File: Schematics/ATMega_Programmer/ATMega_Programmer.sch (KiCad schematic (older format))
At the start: 22 parts, among them U1 74HC04, U2 ATmega644PA, U3 74HC04, U4 28C256, U5 74HC595, U6 74HC00, U7 74LVC1G157, U8 74LVC1G157, U9 74LVC1G126, Y1 20MHz

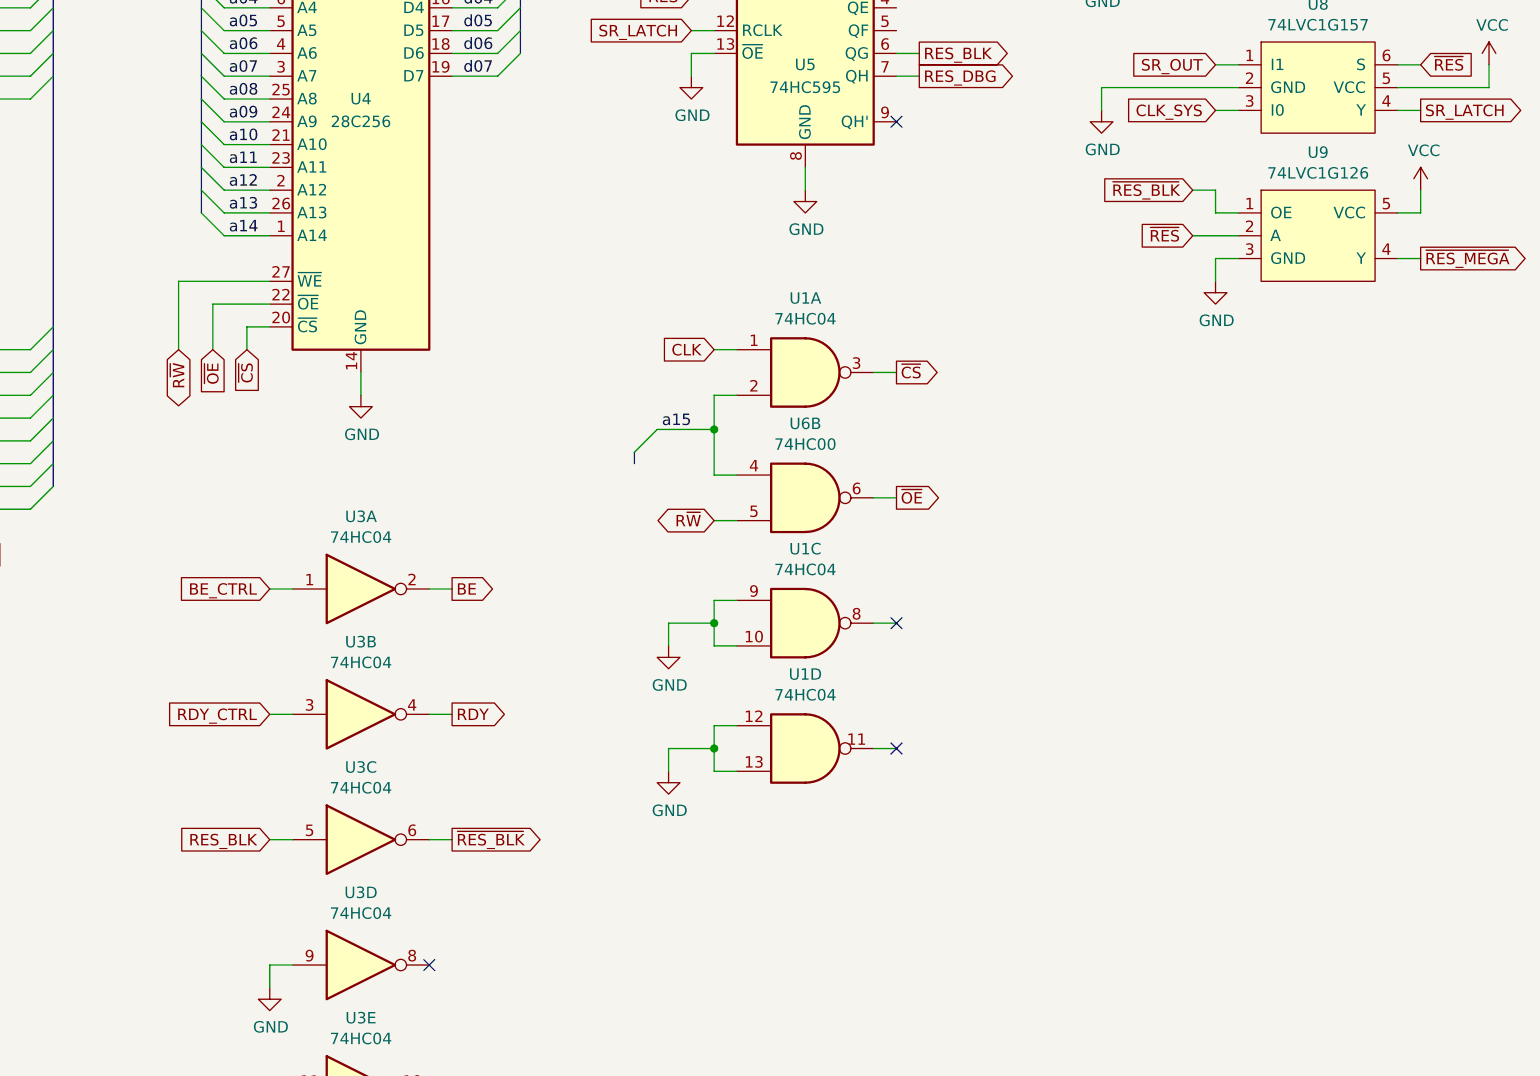
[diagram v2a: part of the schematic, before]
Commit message: Changed 74LVC1G126 to 74LVC1G125 for low-active OE
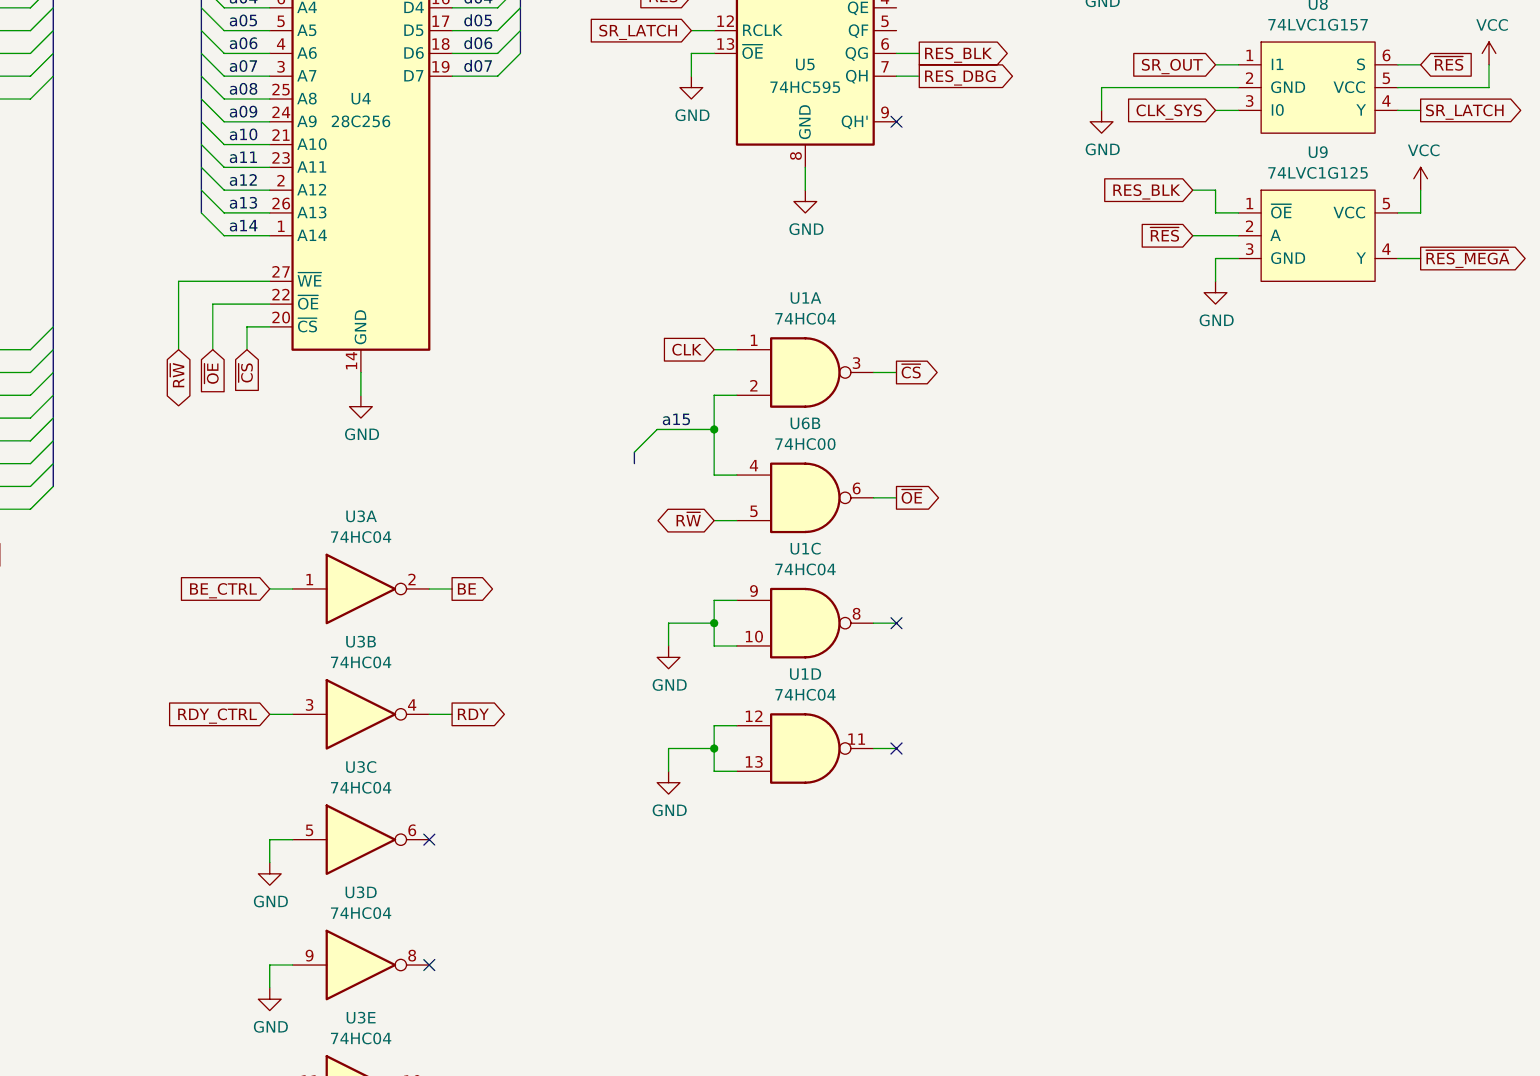
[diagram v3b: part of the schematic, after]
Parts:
- removed U7, U8: 74LVC1G157, Package_SO:SC-74-6_1.5x2.9mm_P0.95mm, symbol 74LVC1G157:74LVC1G157
- removed U9: 74LVC1G126, Package_SO:SC-74-6_1.5x2.9mm_P0.95mm, symbol 74LVC1G126:74LVC1G126
- added U7, U8: 74LVC1G157, Package_SO:SC-74-6_1.5x2.9mm_P0.95mm, symbol 74LVC1G:74LVC1G157
- added U9: 74LVC1G125, Package_SO:SC-74-6_1.5x2.9mm_P0.95mm, symbol 74LVC1G:74LVC1G125
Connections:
- net CLK: now also U7.4 (Y)
- net CLKSEL: now also U7.6 (S)
- net CLK_DBG: now also U7.1 (I1)
- net CLK_SYS: now also U7.3 (I0), U8.3 (I0)
- net GND: now also U3.5, U7.2 (GND), U8.2 (GND), U9.3 (GND)
- net RES_BLK: now also U9.1 (~OE); no longer U3.5
- net SR_LATCH: now also U8.4 (Y)
- net SR_OUT: now also U8.1 (I1)
- net VCC: now also U7.5 (VCC), U8.5 (VCC), U9.5 (VCC)
- net ~RES: now also U8.6 (S), U9.2 (A)
- net ~RES_MEGA: now also U9.4 (Y)
- net ~RES_BLK: no longer names the net of U3.6
- no-connect marks 6 -> 7
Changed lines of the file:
@@
 $EndComp
 $Comp
-L power:GND #PWR015
+L power:GND #PWR016
 U 1 1 5F38A5CE
 P 5550 3350
-F 0 "#PWR015" H 5550 3100 50  0001 C CNN
+F 0 "#PWR016" H 5550 3100 50  0001 C CNN
 F 1 "GND" H 5555 3177 50  0000 C CNN
 F 2 "" H 5550 3350 50  0001 C CNN
@@
 	2850 950  2850 850
 $Comp
-L power:VCC #PWR014
+L power:VCC #PWR015
 U 1 1 5F39AD33
 P 5550 950
-F 0 "#PWR014" H 5550 800 50  0001 C CNN
+F 0 "#PWR015" H 5550 800 50  0001 C CNN
 F 1 "VCC" H 5565 1123 50  0000 C CNN
 F 2 "" H 5550 950 50  0001 C CNN
@@
 NoConn ~ 7900 2150
 $Comp
-L power:VCC #PWR019
+L power:VCC #PWR020
 U 1 1 5F48B33E
 P 7500 950
-F 0 "#PWR019" H 7500 800 50  0001 C CNN
+F 0 "#PWR020" H 7500 800 50  0001 C CNN
 F 1 "VCC" H 7515 1123 50  0000 C CNN
 F 2 "" H 7500 950 50  0001 C CNN
@@
 $EndComp
 $Comp
-L power:GND #PWR020
+L power:GND #PWR021
 U 1 1 5F48B8D8
 P 7500 2450
-F 0 "#PWR020" H 7500 2200 50  0001 C CNN
+F 0 "#PWR021" H 7500 2200 50  0001 C CNN
 F 1 "GND" H 7505 2277 50  0000 C CNN
 F 2 "" H 7500 2450 50  0001 C CNN
@@
 SR_OUT
 $Comp
-L power:GND #PWR018
+L power:GND #PWR019
 U 1 1 5F4E254E
 P 7000 1950
-F 0 "#PWR018" H 7000 1700 50  0001 C CNN
+F 0 "#PWR019" H 7000 1700 50  0001 C CNN
 F 1 "GND" H 7005 1777 50  0000 C CNN
 F 2 "" H 7000 1950 50  0001 C CNN
@@
 NoConn ~ 5850 6950
 $Comp
-L power:GND #PWR011
+L power:GND #PWR012
 U 1 1 5F6D9C6B
 P 5150 5950
-F 0 "#PWR011" H 5150 5700 50  0001 C CNN
+F 0 "#PWR012" H 5150 5700 50  0001 C CNN
 F 1 "GND" H 5155 5777 50  0000 C CNN
 F 2 "" H 5150 5950 50  0001 C CNN
@@
 $EndComp
 $Comp
-L power:GND #PWR012
+L power:GND #PWR013
 U 1 1 5F6DA06D
 P 5150 6500
-F 0 "#PWR012" H 5150 6250 50  0001 C CNN
+F 0 "#PWR013" H 5150 6250 50  0001 C CNN
 F 1 "GND" H 5155 6327 50  0000 C CNN
 F 2 "" H 5150 6500 50  0001 C CNN
@@
 $EndComp
 $Comp
-L power:GND #PWR013
+L power:GND #PWR014
 U 1 1 5F6DA68F
 P 5150 7050
-F 0 "#PWR013" H 5150 6800 50  0001 C CNN
+F 0 "#PWR014" H 5150 6800 50  0001 C CNN
 F 1 "GND" H 5155 6877 50  0000 C CNN
 F 2 "" H 5150 7050 50  0001 C CNN
@@
 	5150 6950 5250 6950
 $Comp
-L power:GND #PWR016
+L power:GND #PWR017
 U 1 1 5F6FA13A
 P 6900 4450
-F 0 "#PWR016" H 6900 4200 50  0001 C CNN
+F 0 "#PWR017" H 6900 4200 50  0001 C CNN
 F 1 "GND" H 6905 4277 50  0000 C CNN
 F 2 "" H 6900 4450 50  0001 C CNN
@@
 $EndComp
 $Comp
-L power:GND #PWR017
+L power:GND #PWR018
 U 1 1 5F6FA77D
 P 6900 5000
-F 0 "#PWR017" H 6900 4750 50  0001 C CNN
+F 0 "#PWR018" H 6900 4750 50  0001 C CNN
 F 1 "GND" H 6905 4827 50  0000 C CNN
 F 2 "" H 6900 5000 50  0001 C CNN
@@
 NoConn ~ 7900 4350
 NoConn ~ 7900 4900
-$Comp
-L 74LVC1G157:74LVC1G157 U7
-U 1 1 5F7A7711
-P 9750 1350
-F 0 "U7" H 9750 1715 50  0000 C CNN
-F 1 "74LVC1G157" H 9750 1624 50  0000 C CNN
-F 2 "Package_SO:SC-74-6_1.5x2.9mm_P0.95mm" H 9700 1250 50  0001 C CNN
-F 3 "" H 9700 1250 50  0001 C CNN
-	1    9750 1350
-	1    0    0    -1
-$EndComp
 Text GLabel 9300 1250 0    50   Input ~ 0
 CLK_DBG
 $Comp
-L power:GND #PWR021
+L power:GND #PWR022
 U 1 1 5F7A8816
 P 8800 1450
-F 0 "#PWR021" H 8800 1200 50  0001 C CNN
+F 0 "#PWR022" H 8800 1200 50  0001 C CNN
 F 1 "GND" H 8805 1277 50  0000 C CNN
 F 2 "" H 8800 1450 50  0001 C CNN
@@
 	10100 1250 10200 1250
 $Comp
-L power:VCC #PWR025
+L power:VCC #PWR027
 U 1 1 5F7CB4D9
 P 10650 1250
-F 0 "#PWR025" H 10650 1100 50  0001 C CNN
+F 0 "#PWR027" H 10650 1100 50  0001 C CNN
 F 1 "VCC" H 10665 1423 50  0000 C CNN
 F 2 "" H 10650 1250 50  0001 C CNN
@@
 Wire Wire Line
 	10100 1450 10200 1450
-$Comp
-L 74LVC1G157:74LVC1G157 U8
-U 1 1 5F7DE350
-P 9750 2000
-F 0 "U8" H 9750 2365 50  0000 C CNN
-F 1 "74LVC1G157" H 9750 2274 50  0000 C CNN
-F 2 "Package_SO:SC-74-6_1.5x2.9mm_P0.95mm" H 9700 1900 50  0001 C CNN
-F 3 "" H 9700 1900 50  0001 C CNN
-	1    9750 2000
-	1    0    0    -1
-$EndComp
 Text GLabel 9300 2100 0    50   Input ~ 0
 CLK_SYS
 $Comp
-L power:GND #PWR022
+L power:GND #PWR023
 U 1 1 5F7DEA14
 P 8800 2100
-F 0 "#PWR022" H 8800 1850 50  0001 C CNN
+F 0 "#PWR023" H 8800 1850 50  0001 C CNN
 F 1 "GND" H 8805 1927 50  0000 C CNN
 F 2 "" H 8800 2100 50  0001 C CNN
@@
 	1100 1150 1100 1550
 Connection ~ 1100 1550
-$Comp
-L 74LVC1G126:74LVC1G126 U9
-U 1 1 5F9A8205
-P 9750 2650
-F 0 "U9" H 9750 3015 50  0000 C CNN
-F 1 "74LVC1G126" H 9750 2924 50  0000 C CNN
-F 2 "Package_SO:SC-74-6_1.5x2.9mm_P0.95mm" H 9700 2400 50  0001 C CNN
-F 3 "" H 9700 2550 50  0001 C CNN
-	1    9750 2650
-	1    0    0    -1
-$EndComp
 Text GLabel 8000 1850 2    50   Output ~ 0
 RES_BLK
 Wire Wire Line
 	7900 1850 8000 1850
-Text GLabel 5150 5300 0    50   Input ~ 0
+Text GLabel 9200 2450 0    50   Input ~ 0
 RES_BLK
-Text GLabel 5950 5300 2    50   Output ~ 0
-~RES_BLK
-Wire Wire Line
-	5850 5300 5950 5300
-Text GLabel 9200 2450 0    50   Input ~ 0
-~RES_BLK
 Wire Wire Line
 	9200 2450 9300 2450
@@
 	9300 2550 9400 2550
 $Comp
-L power:GND #PWR023
+L power:GND #PWR024
 U 1 1 5F9EDE67
 P 9300 2850
-F 0 "#PWR023" H 9300 2600 50  0001 C CNN
+F 0 "#PWR024" H 9300 2600 50  0001 C CNN
 F 1 "GND" H 9305 2677 50  0000 C CNN
 F 2 "" H 9300 2850 50  0001 C CNN
@@
 	9300 2750 9400 2750
 $Comp
-L power:VCC #PWR024
+L power:VCC #PWR025
 U 1 1 5F9FA794
 P 10200 2450
-F 0 "#PWR024" H 10200 2300 50  0001 C CNN
+F 0 "#PWR025" H 10200 2300 50  0001 C CNN
 F 1 "VCC" H 10215 2623 50  0000 C CNN
 F 2 "" H 10200 2450 50  0001 C CNN
@@
 	1    0    0    -1
 $EndComp
+$Comp
+L power:GND #PWR011
+U 1 1 5F420776
+P 5150 5400
+F 0 "#PWR011" H 5150 5150 50  0001 C CNN
+F 1 "GND" H 5155 5227 50  0000 C CNN
+F 2 "" H 5150 5400 50  0001 C CNN
+F 3 "" H 5150 5400 50  0001 C CNN
+	1    5150 5400
+	1    0    0    -1
+$EndComp
+Wire Wire Line
+	5150 5400 5150 5300
+NoConn ~ 5850 5300
+$Comp
+L 74LVC1G:74LVC1G157 U7
+U 1 1 5F445EA1
+P 9750 1350
+F 0 "U7" H 9750 1715 50  0000 C CNN
+F 1 "74LVC1G157" H 9750 1624 50  0000 C CNN
+F 2 "Package_SO:SC-74-6_1.5x2.9mm_P0.95mm" H 9700 1100 50  0001 C CNN
+F 3 "" H 9700 1250 50  0001 C CNN
+	1    9750 1350
+	1    0    0    -1
+$EndComp
+$Comp
+L 74LVC1G:74LVC1G157 U8
+U 1 1 5F446754
+P 9750 2000
+F 0 "U8" H 9750 2365 50  0000 C CNN
+F 1 "74LVC1G157" H 9750 2274 50  0000 C CNN
+F 2 "Package_SO:SC-74-6_1.5x2.9mm_P0.95mm" H 9700 1750 50  0001 C CNN
+F 3 "" H 9700 1900 50  0001 C CNN
+	1    9750 2000
+	1    0    0    -1
+$EndComp
+$Comp
+L 74LVC1G:74LVC1G125 U9
+U 1 1 5F447644
+P 9750 2650
+F 0 "U9" H 9750 3015 50  0000 C CNN
+F 1 "74LVC1G125" H 9750 2924 50  0000 C CNN
+F 2 "Package_SO:SC-74-6_1.5x2.9mm_P0.95mm" H 9700 2400 50  0001 C CNN
+F 3 "" H 9700 2550 50  0001 C CNN
+	1    9750 2650
+	1    0    0    -1
+$EndComp

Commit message: Updates to schematic
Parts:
- removed U9: 74LVC1G125, Package_SO:SC-74-6_1.5x2.9mm_P0.95mm, symbol 74LVC1G:74LVC1G125
- added Q?: 2N3904, Package_TO_SOT_THT:TO-92_Inline, symbol Transistor_BJT:2N3904
- added U?: 74LVC1G07, Package_TO_SOT_SMD:SOT-353_SC-70-5_Handsoldering, symbol 74LVC1G:74LVC1G07
- U1: value 74HC04 -> 74HC00
- renumbered U6 to U1, U7 to U6, U8 to U7
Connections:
- net ~RES_MEGA is gone; now on net ~RES: U2.9 (~RESET)
- net GND: now also Q?.1 (E), U?.3 (GND)
- net RES_DBG: now also Q?.2 (B)
- net VCC: now also U?.5 (VCC)
- net ~RES: now also U?.2 (A)
- net RES_BLK: no longer names the net of U5.6 (QG)
- new net ~6502_RES: U?.4 (Y)
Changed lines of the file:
@@
 Text Label 3500 2950 0    50   ~ 0
 d07
-Text GLabel 9200 2650 0    50   Input ~ 0
-~RES
 Text GLabel 3550 4050 2    50   Input ~ 0
 RxD_DBG
@@
 P 7500 3250
 F 0 "U1" H 7500 3575 50  0000 C CNN
-F 1 "74HC04" H 7500 3484 50  0000 C CNN
+F 1 "74HC00" H 7500 3484 50  0000 C CNN
 F 2 "" H 7500 3250 50  0001 C CNN
-F 3 "https://assets.nexperia.com/documents/data-sheet/74HC_HCT04.pdf" H 7500 3250 50  0001 C CNN
+F 3 "" H 7500 3250 50  0001 C CNN
 	1    7500 3250
 	1    0    0    -1
@@
 P 2400 6550
 F 0 "U1" H 2630 6596 50  0000 L CNN
-F 1 "74HC04" H 2630 6505 50  0000 L CNN
+F 1 "74HC00" H 2630 6505 50  0000 L CNN
 F 2 "" H 2400 6550 50  0001 C CNN
-F 3 "https://assets.nexperia.com/documents/data-sheet/74HC_HCT04.pdf" H 2400 6550 50  0001 C CNN
+F 3 "" H 2400 6550 50  0001 C CNN
 	5    2400 6550
 	1    0    0    -1
@@
 	2400 5950 2400 6050
 $Comp
-L 74xx:74HC00 U6
+L 74xx:74HC00 U1
 U 2 1 5F371287
 P 7500 3800
-F 0 "U6" H 7500 4125 50  0000 C CNN
+F 0 "U1" H 7500 4125 50  0000 C CNN
 F 1 "74HC00" H 7500 4034 50  0000 C CNN
 F 2 "" H 7500 3800 50  0001 C CNN
@@
 P 7500 4350
 F 0 "U1" H 7500 4675 50  0000 C CNN
-F 1 "74HC04" H 7500 4584 50  0000 C CNN
+F 1 "74HC00" H 7500 4584 50  0000 C CNN
 F 2 "" H 7500 4350 50  0001 C CNN
-F 3 "https://assets.nexperia.com/documents/data-sheet/74HC_HCT04.pdf" H 7500 4350 50  0001 C CNN
+F 3 "" H 7500 4350 50  0001 C CNN
 	3    7500 4350
 	1    0    0    -1
@@
 P 7500 4900
 F 0 "U1" H 7500 5225 50  0000 C CNN
-F 1 "74HC04" H 7500 5134 50  0000 C CNN
+F 1 "74HC00" H 7500 5134 50  0000 C CNN
 F 2 "" H 7500 4900 50  0001 C CNN
-F 3 "https://assets.nexperia.com/documents/data-sheet/74HC_HCT04.pdf" H 7500 4900 50  0001 C CNN
+F 3 "" H 7500 4900 50  0001 C CNN
 	4    7500 4900
 	1    0    0    -1
@@
 	1100 1150 1100 1550
 Connection ~ 1100 1550
-Text GLabel 8000 1850 2    50   Output ~ 0
-RES_BLK
 Wire Wire Line
 	7900 1850 8000 1850
-Text GLabel 9200 2450 0    50   Input ~ 0
-RES_BLK
-Wire Wire Line
-	9200 2450 9300 2450
-Wire Wire Line
-	9300 2450 9300 2550
-Wire Wire Line
-	9300 2550 9400 2550
-$Comp
-L power:GND #PWR024
-U 1 1 5F9EDE67
-P 9300 2850
-F 0 "#PWR024" H 9300 2600 50  0001 C CNN
-F 1 "GND" H 9305 2677 50  0000 C CNN
-F 2 "" H 9300 2850 50  0001 C CNN
-F 3 "" H 9300 2850 50  0001 C CNN
-	1    9300 2850
-	1    0    0    -1
-$EndComp
-Wire Wire Line
-	9300 2850 9300 2750
-Wire Wire Line
-	9300 2750 9400 2750
-$Comp
-L power:VCC #PWR025
-U 1 1 5F9FA794
-P 10200 2450
-F 0 "#PWR025" H 10200 2300 50  0001 C CNN
-F 1 "VCC" H 10215 2623 50  0000 C CNN
-F 2 "" H 10200 2450 50  0001 C CNN
-F 3 "" H 10200 2450 50  0001 C CNN
-	1    10200 2450
-	1    0    0    -1
-$EndComp
-Wire Wire Line
-	10200 2450 10200 2550
-Wire Wire Line
-	10200 2550 10100 2550
-Wire Wire Line
-	9200 2650 9400 2650
-Text GLabel 10200 2750 2    50   Output ~ 0
-~RES_MEGA
-Wire Wire Line
-	10100 2750 10200 2750
 Text GLabel 2150 1350 0    50   Input ~ 0
-~RES_MEGA
+~RES
 Wire Wire Line
 	3200 6050 3200 5950
@@
 NoConn ~ 5850 5300
 $Comp
-L 74LVC1G:74LVC1G157 U7
+L 74LVC1G:74LVC1G157 U6
 U 1 1 5F445EA1
 P 9750 1350
-F 0 "U7" H 9750 1715 50  0000 C CNN
+F 0 "U6" H 9750 1715 50  0000 C CNN
 F 1 "74LVC1G157" H 9750 1624 50  0000 C CNN
 F 2 "Package_SO:SC-74-6_1.5x2.9mm_P0.95mm" H 9700 1100 50  0001 C CNN
@@
 $EndComp
 $Comp
-L 74LVC1G:74LVC1G157 U8
+L 74LVC1G:74LVC1G157 U7
 U 1 1 5F446754
 P 9750 2000
-F 0 "U8" H 9750 2365 50  0000 C CNN
+F 0 "U7" H 9750 2365 50  0000 C CNN
 F 1 "74LVC1G157" H 9750 2274 50  0000 C CNN
 F 2 "Package_SO:SC-74-6_1.5x2.9mm_P0.95mm" H 9700 1750 50  0001 C CNN
@@
 $EndComp
 $Comp
-L 74LVC1G:74LVC1G125 U9
-U 1 1 5F447644
+L 74LVC1G:74LVC1G07 U?
+U 1 1 5F48C039
 P 9750 2650
-F 0 "U9" H 9750 3015 50  0000 C CNN
-F 1 "74LVC1G125" H 9750 2924 50  0000 C CNN
-F 2 "Package_SO:SC-74-6_1.5x2.9mm_P0.95mm" H 9700 2400 50  0001 C CNN
+F 0 "U?" H 9750 3015 50  0000 C CNN
+F 1 "74LVC1G07" H 9750 2924 50  0000 C CNN
+F 2 "Package_TO_SOT_SMD:SOT-353_SC-70-5_Handsoldering" H 9700 2400 50  0001 C CNN
 F 3 "" H 9700 2550 50  0001 C CNN
 	1    9750 2650
 	1    0    0    -1
 $EndComp
+Text GLabel 9300 2650 0    50   Input ~ 0
+~RES
+Wire Wire Line
+	9300 2650 9400 2650
+$Comp
+L power:GND #PWR?
+U 1 1 5F498153
+P 9300 2850
+F 0 "#PWR?" H 9300 2600 50  0001 C CNN
+F 1 "GND" H 9305 2677 50  0000 C CNN
+F 2 "" H 9300 2850 50  0001 C CNN
+F 3 "" H 9300 2850 50  0001 C CNN
+	1    9300 2850
+	1    0    0    -1
+$EndComp
+$Comp
+L power:VCC #PWR?
+U 1 1 5F498E5D
+P 10200 2450
+F 0 "#PWR?" H 10200 2300 50  0001 C CNN
+F 1 "VCC" H 10215 2623 50  0000 C CNN
+F 2 "" H 10200 2450 50  0001 C CNN
+F 3 "" H 10200 2450 50  0001 C CNN
+	1    10200 2450
+	1    0    0    -1
+$EndComp
+Wire Wire Line
+	9300 2850 9300 2750
+Wire Wire Line
+	9300 2750 9400 2750
+Wire Wire Line
+	10100 2550 10200 2550
+Wire Wire Line
+	10200 2550 10200 2450
+$Comp
+L Transistor_BJT:2N3904 Q?
+U 1 1 5F4B1949
+P 10200 3350
+F 0 "Q?" H 10390 3396 50  0000 L CNN
+F 1 "2N3904" H 10390 3305 50  0000 L CNN
+F 2 "Package_TO_SOT_THT:TO-92_Inline" H 10400 3275 50  0001 L CIN
+F 3 "https://www.fairchildsemi.com/datasheets/2N/2N3904.pdf" H 10200 3350 50  0001 L CNN
+	1    10200 3350
+	1    0    0    -1
+$EndComp
+Text GLabel 9900 3350 0    50   Input ~ 0
+RES_DBG
+Wire Wire Line
+	9900 3350 10000 3350
+Wire Wire Line
+	10100 2750 10300 2750
+Wire Wire Line
+	10300 2750 10300 2850
+$Comp
+L power:GND #PWR?
+U 1 1 5F4D0164
+P 10300 3650
+F 0 "#PWR?" H 10300 3400 50  0001 C CNN
+F 1 "GND" H 10305 3477 50  0000 C CNN
+F 2 "" H 10300 3650 50  0001 C CNN
+F 3 "" H 10300 3650 50  0001 C CNN
+	1    10300 3650
+	1    0    0    -1
+$EndComp
+Wire Wire Line
+	10300 3550 10300 3650
+Text GLabel 10400 2750 2    50   Output ~ 0
+~6502_RES
+Wire Wire Line
+	10300 2750 10400 2750
+Connection ~ 10300 2750
 Wire Bus Line
 	3800 2150 3800 2850
